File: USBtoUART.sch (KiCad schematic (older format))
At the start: 19 parts, among them J4 UJ2-MIBH-4-SMT-TR, U1 FT2232D-REEL, Y1 AS-6.000-12-2020-EXT-SMD-TR

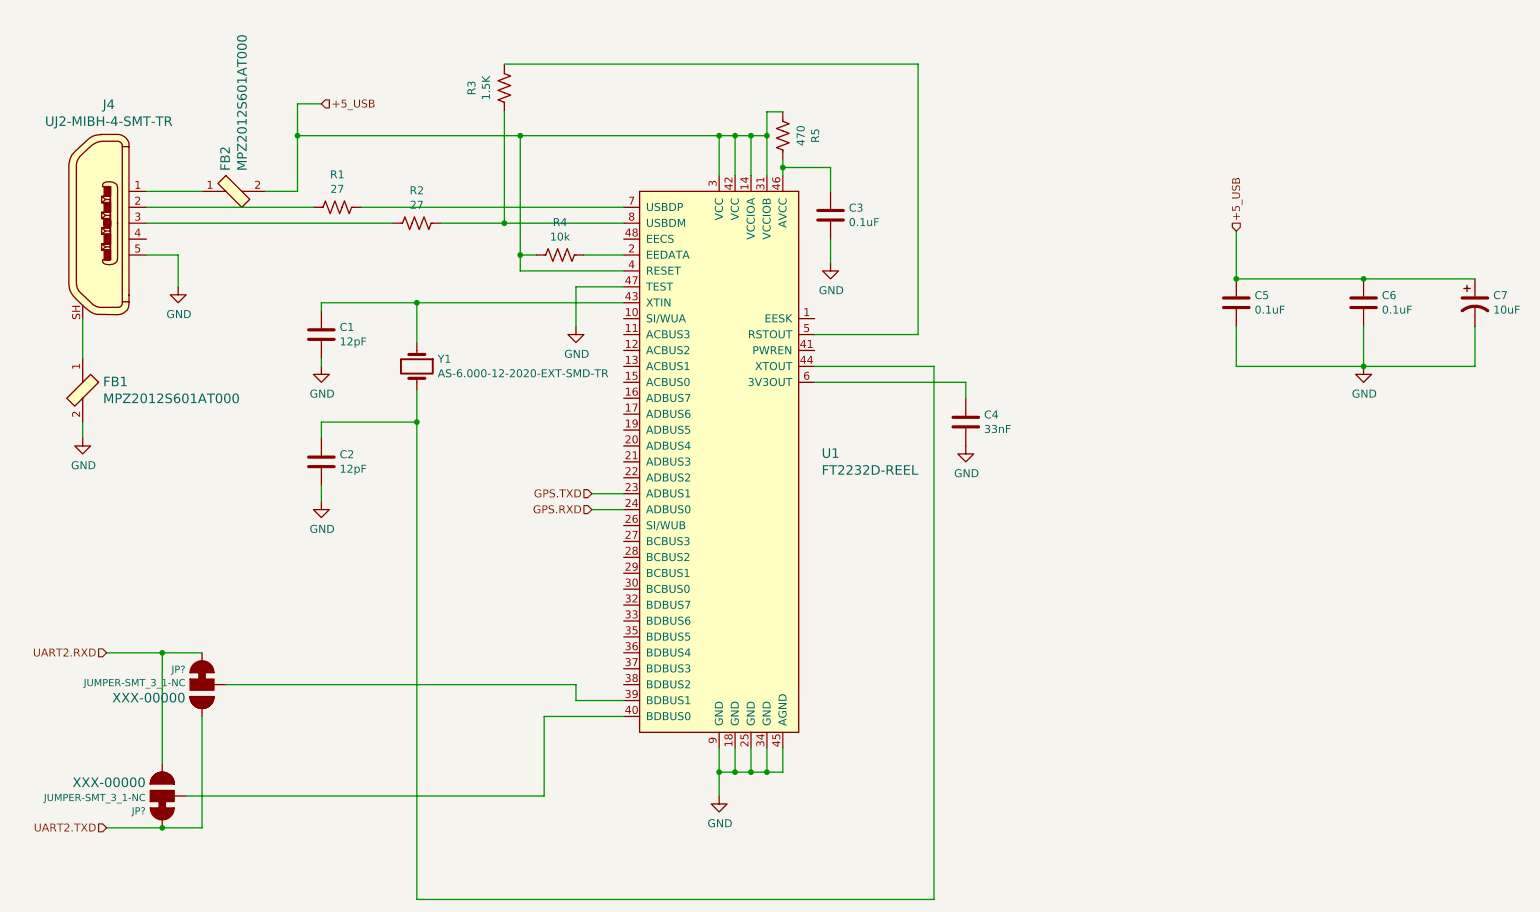
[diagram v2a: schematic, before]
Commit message: eFuse added
Added eFuse, LEDs, and addtional power configuration options.
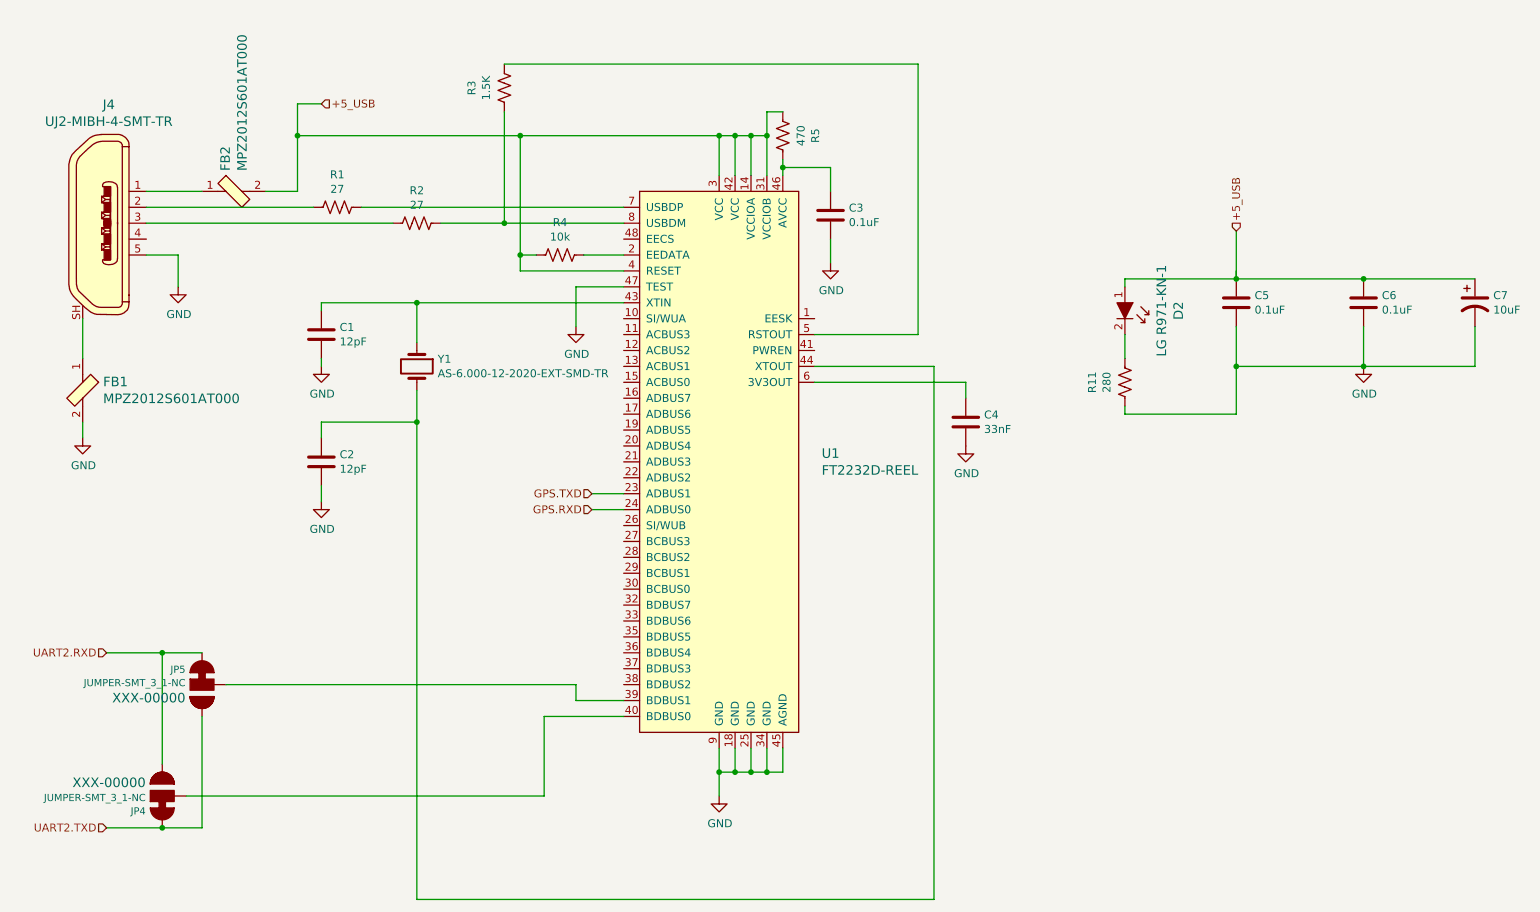
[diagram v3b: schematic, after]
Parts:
- added D2: LG R971-KN-1, digikey-footprints:0805, symbol dk_LED-Indication-Discrete:LH_R974-LP-1
- added R11: 280, Resistor_SMD:R_0805_2012Metric_Pad1.20x1.40mm_HandSolder, symbol Device:R_US
- gave numbers to parts that had none: 2
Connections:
- net +5_USB: now also D2.1
- net GND: now also R11.2
- new net: D2.2, R11.1
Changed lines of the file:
@@
 EELAYER 30 0
 EELAYER END
-$Descr A4 11693 8268
+$Descr USLetter 11000 8500
 encoding utf-8
-Sheet 2 4
-Title ""
-Date ""
-Rev ""
+Sheet 2 5
+Title "USB to UART"
+Date "2020-10-17"
+Rev "2"
 Comp ""
 Comment1 ""
@@
 +5_USB
 Wire Wire Line
-	8500 2150 8500 2450
-Wire Wire Line
 	8500 2450 9300 2450
 Connection ~ 8500 2450
@@
 U 1 1 5F8D37AA
 P 2000 5000
-F 0 "JP?" H 2104 4905 45  0000 L CNN
+AR Path="/5F7C6408/5F8D37AA" Ref="JP?"  Part="1"
+AR Path="/5F8460BD/5F8D37AA" Ref="JP5"  Part="1"
+F 0 "JP5" H 2104 4905 45  0000 L CNN
 F 1 "JUMPER-SMT_3_1-NC" H 2104 4989 45  0000 L CNN
 F 2 "SMT-JUMPER_3_1-NC" H 2000 5250 20  0001 C CNN
@@
 U 1 1 5F8DF40E
 P 1750 5700
-F 0 "JP?" H 1854 5605 45  0000 L CNN
+AR Path="/5F7C6408/5F8DF40E" Ref="JP?"  Part="1"
+AR Path="/5F8460BD/5F8DF40E" Ref="JP4"  Part="1"
+F 0 "JP4" H 1854 5605 45  0000 L CNN
 F 1 "JUMPER-SMT_3_1-NC" H 1854 5689 45  0000 L CNN
 F 2 "SMT-JUMPER_3_1-NC" H 1750 5950 20  0001 C CNN
@@
 Wire Wire Line
 	1750 4800 1400 4800
+$Comp
+L dk_LED-Indication-Discrete:LH_R974-LP-1 D?
+U 1 1 5F9390C2
+P 7800 2700
+AR Path="/5F917C06/5F9390C2" Ref="D?"  Part="1"
+AR Path="/5F8460BD/5F9390C2" Ref="D2"  Part="1"
+F 0 "D2" H 7750 3037 60  0000 C CNN
+F 1 "LG R971-KN-1" H 7750 2931 60  0000 C CNN
+F 2 "digikey-footprints:0805" H 8000 2900 60  0001 L CNN
+F 3 "https://dammedia.osram.info/media/resource/hires/osram-dam-2493888/LH%20R974.pdf" H 8000 3000 60  0001 L CNN
+F 4 "475-1410-1-ND" H 8000 3100 60  0001 L CNN "Digi-Key_PN"
+F 5 "LG R971-KN-1" H 8000 3200 60  0001 L CNN "MPN"
+F 6 "Optoelectronics" H 8000 3300 60  0001 L CNN "Category"
+F 7 "LED Indication - Discrete" H 8000 3400 60  0001 L CNN "Family"
+F 8 "https://dammedia.osram.info/media/resource/hires/osram-dam-2493888/LH%20R974.pdf" H 8000 3500 60  0001 L CNN "DK_Datasheet_Link"
+F 9 "/product-detail/en/osram-opto-semiconductors-inc/LH-R974-LP-1/475-1415-1-ND/1802604" H 8000 3600 60  0001 L CNN "DK_Detail_Page"
+F 10 "LED GREEN DIFFUSED 0805 SMD" H 8000 3700 60  0001 L CNN "Description"
+F 11 "OSRAM Opto Semiconductors Inc." H 8000 3800 60  0001 L CNN "Manufacturer"
+F 12 "Active" H 8000 3900 60  0001 L CNN "Status"
+	1    7800 2700
+	0    1    1    0
+$EndComp
+$Comp
+L Device:R_US R11
+U 1 1 5F9390CA
+P 7800 3100
+AR Path="/5F8460BD/5F9390CA" Ref="R11"  Part="1"
+AR Path="/5F917C06/5F9390CA" Ref="R?"  Part="1"
+F 0 "R11" V 7595 3100 50  0000 C CNN
+F 1 "280" V 7686 3100 50  0000 C CNN
+F 2 "Resistor_SMD:R_0805_2012Metric_Pad1.20x1.40mm_HandSolder" V 7840 3090 50  0001 C CNN
+F 3 "https://www.yageo.com/upload/media/product/productsearch/datasheet/rchip/PYu-RC_Group_51_RoHS_L_11.pdf" H 7800 3100 50  0001 C CNN
+F 4 "Yageo" V 7800 3100 50  0001 C CNN "Manufacturer"
+F 5 "RC0805FR-07280RL" V 7800 3100 50  0001 C CNN "MPN"
+	1    7800 3100
+	1    0    0    -1
+$EndComp
+Wire Wire Line
+	7800 2950 7800 2800
+Wire Wire Line
+	7800 2500 7800 2450
+Wire Wire Line
+	7800 2450 8500 2450
+Wire Wire Line
+	8500 2400 8500 2450
+Wire Wire Line
+	8500 2150 8500 2450
+Wire Wire Line
+	7800 3250 7800 3300
+Wire Wire Line
+	7800 3300 8500 3300
+Wire Wire Line
+	8500 3300 8500 3000
+Connection ~ 8500 3000
 $EndSCHEMATC
